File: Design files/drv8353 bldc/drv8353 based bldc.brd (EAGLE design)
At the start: 177.8 x 127.8 mm, 125 parts, among them IC1 DRV8353RSRGZT, J3 2X6 FEMALE, J4 B06B-HCMKK

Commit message: changes
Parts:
- moved C27 128.0 mm to (82.9, 42.8), turned to 270 degrees
- moved C28 124.0 mm to (80.7, 46.2)
- moved C25 121.0 mm to (108.8, 43.9), turned to 180 degrees
- moved C12 118.0 mm to (109.0, 66.9), turned to 270 degrees
- moved C15 115.1 mm to (95.4, 52.4)
- moved C11 111.4 mm to (103.4, 66.9), turned to 270 degrees
- moved C26 111.0 mm to (109.7, 33.7), turned to 270 degrees
- moved C1 110.5 mm to (74.7, 60.3), turned to 90 degrees
- moved C10 110.3 mm to (101.0, 63.3), turned to 270 degrees
- moved C29 97.2 mm to (75.0, 41.4), turned to 90 degrees
- moved R3 97.2 mm to (72.7, 60.3), turned to 270 degrees
- moved R11 94.3 mm to (105.2, 66.9), turned to 270 degrees
- moved R10 94.3 mm to (102.7, 63.3), turned to 270 degrees
- moved R12 92.2 mm to (107.2, 66.9), turned to 270 degrees
- moved BB2 86.3 mm to (116.8, 9.50)
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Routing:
- net 3V3: track 0.00 -> 87.9 mm, vias 0 -> 3
- net ENABLE: track 0.00 -> 47.9 mm, vias 0 -> 1
- net NFAULT: track 0.00 -> 39.3 mm, vias 0 -> 1
- net MISO: track 0.00 -> 33.0 mm, vias 0 -> 1
- net MOSI: track 0.00 -> 29.8 mm, vias 0 -> 1
- net INLC: track 0.00 -> 25.8 mm
- net INHC: track 0.00 -> 22.7 mm
- net INLB: track 0.00 -> 20.3 mm
- net CS: track 0.00 -> 19.9 mm
- net INHB: track 0.00 -> 18.3 mm
- net INLA: track 0.00 -> 16.9 mm
- net INHA: track 0.00 -> 15.5 mm
- net N$5: track 0.00 -> 10.6 mm
- net SOC: track 0.00 -> 7.83 mm
- net SOB: track 0.00 -> 7.83 mm
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- added copper zone on layer 1, net 3V3
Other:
- board size 177.8 x 127.8 mm -> 145.3 x 127.8 mm

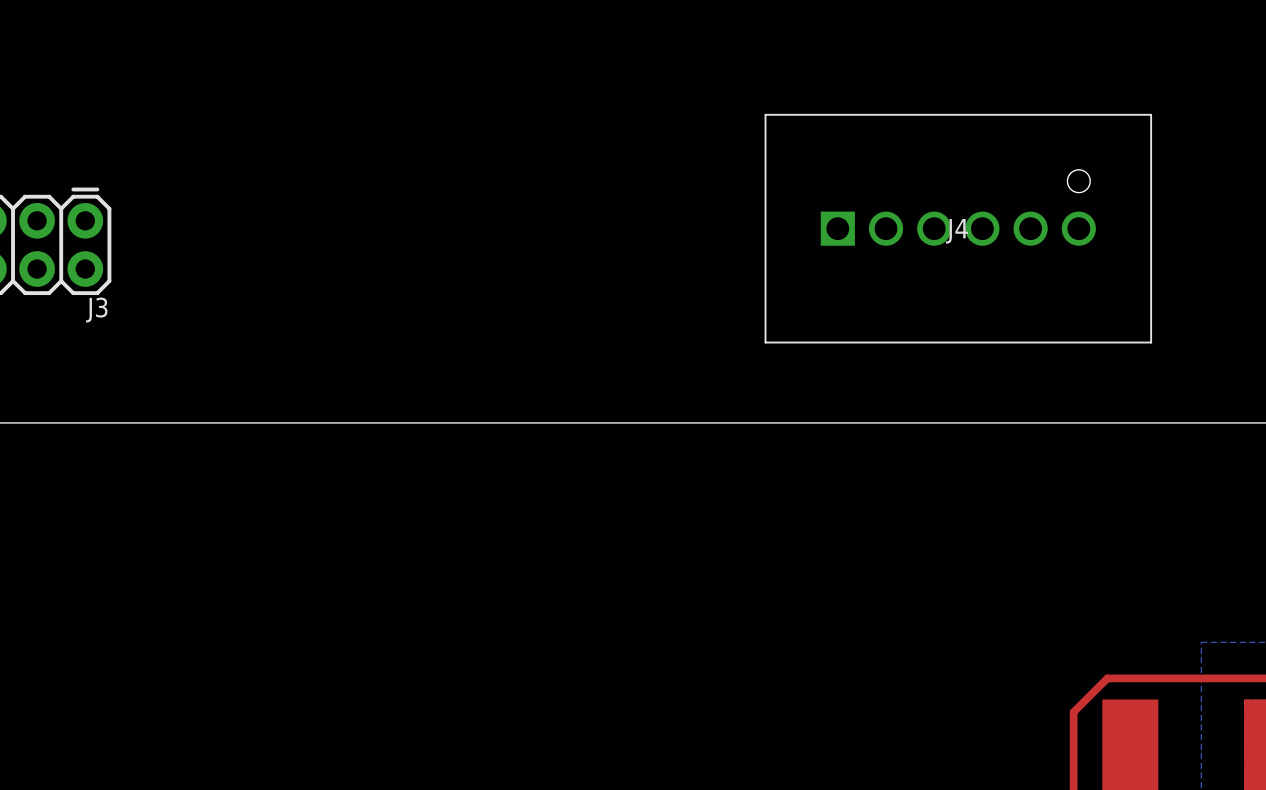
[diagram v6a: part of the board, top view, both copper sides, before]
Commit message: small fix for spi mosi route
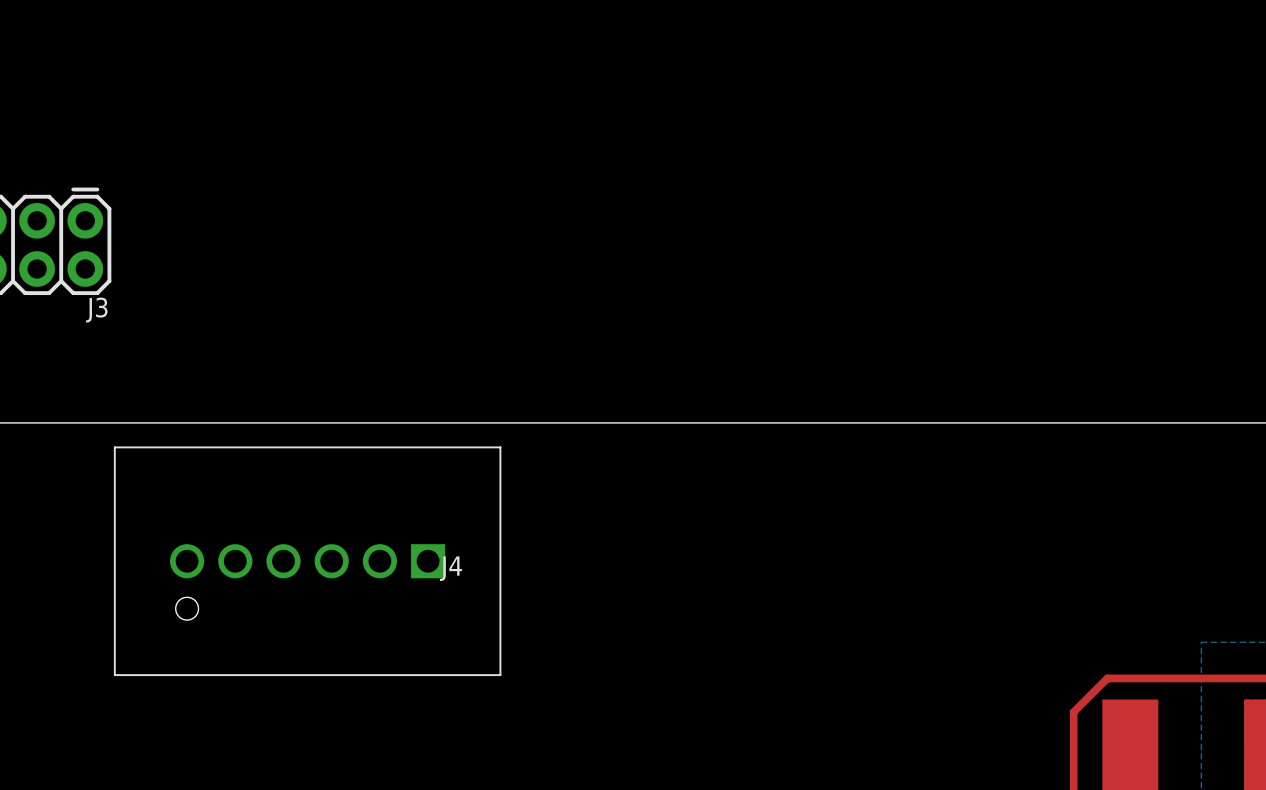
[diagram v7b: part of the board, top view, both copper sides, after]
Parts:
- moved J4 27.8 mm to (90.4, 96.9), turned to 180 degrees
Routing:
- net MISO: track 33.0 -> 34.6 mm

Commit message: adds GND planes, vias
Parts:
- moved R5 143.9 mm to (93.6, 18.2), turned to 180 degrees
- moved L2 137.2 mm to (93.6, 20.1)
- moved R4 102.0 mm to (99.7, 63.3)
- moved L1 91.4 mm to (99.9, 61.4), turned to 180 degrees
- moved C10 3.78 mm to (99.7, 66.9)
- moved R10 3.78 mm to (101.5, 66.9)
- moved F1 0.57 mm to (157.0, 0.96)
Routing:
- net 3V3: track 87.9 -> 84.9 mm
- net GND: vias 1 -> 99
- added copper zone on layer 15, net AGND
- added copper zone on layer 15, net GND
- added copper zone on layer 2, net GND
